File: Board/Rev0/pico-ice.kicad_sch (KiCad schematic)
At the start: 103 parts, among them J1 Connector_USB_B_Micro, J10 2x3_2.54mm_Female, J11 2x3_2.54mm_Female, J3 6X2 Female Header, J4 6X2 Female Header, J5 Conn_ARM_JTAG_SWD_10, J6 6X2 Female Header, J7 6X2 Female Header, J8 6X2 Female Header, J9 BOOT_SEL, SW1 PTS820 J25K SMTR LFS, SW2 PTS820 J25K SMTR LFS, U1 NCP1117ST33T3G, U2 W25Q32JVSSIQ, U3 RP2040, U4 CL9293A12L5M, U5 APS6404L-3SQN-SN, U6 ICE40UP5K-SG48ITR, U8 W25Q32JVSSIQ, Y1 ABLS-12.000MHZ-B4-T

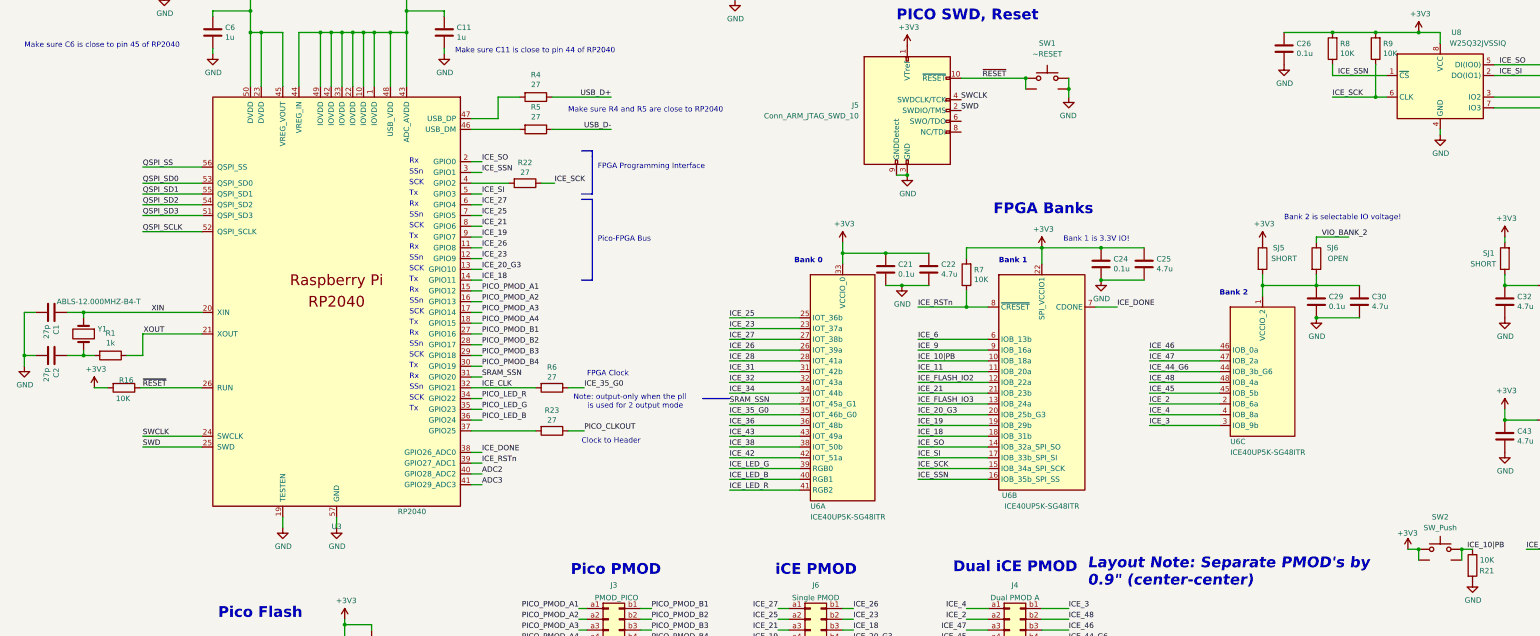
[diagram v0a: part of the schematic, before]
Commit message: Reduce the board outline.
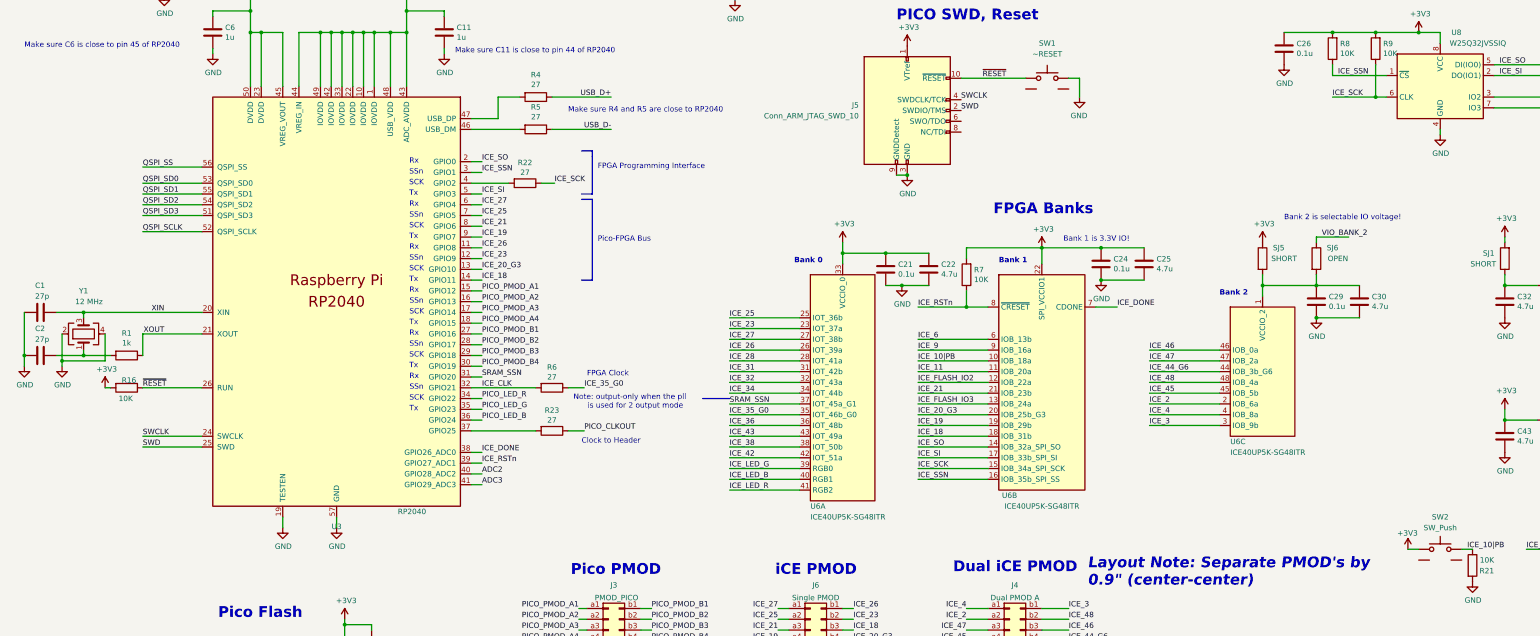
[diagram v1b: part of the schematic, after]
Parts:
- removed Y1: ABLS-12.000MHZ-B4-T, RP2040_minimal:Crystal_SMD_HC49-US, symbol Device:Crystal
- added Y1: 12 MHz, Crystal:Crystal_SMD_2520-4Pin_2.5x2.0mm, symbol Device:Crystal_GND24
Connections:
- net +3V3: no longer SW2.SH1
- net GND: now also Y1.2, Y1.4; no longer SW1.SH1
- net ICE_10|PB: no longer SW2.SH2
- net XIN: now also Y1.3
- net ~{RESET}: no longer SW1.SH2
- net at C2.1, R1.2: now also Y1.1
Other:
- moved on the sheet: C1, C2, R1, R16

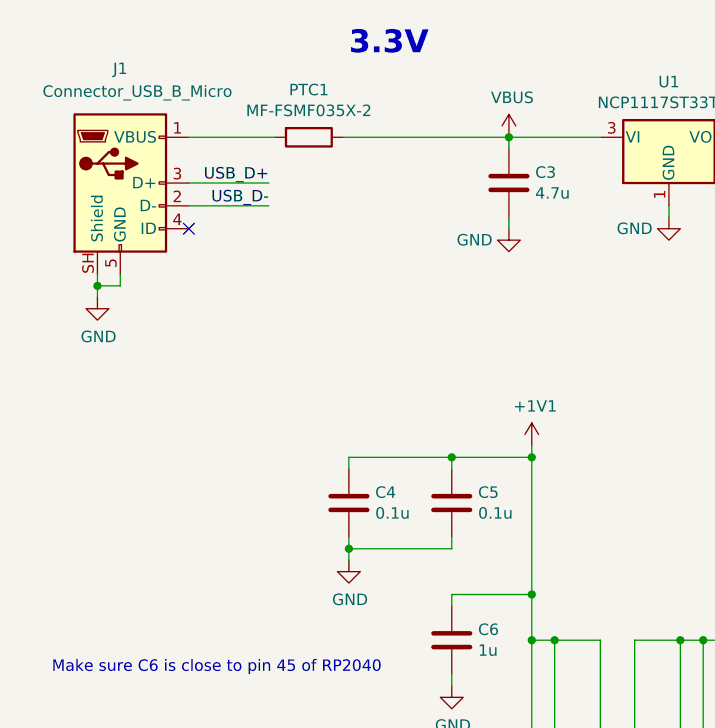
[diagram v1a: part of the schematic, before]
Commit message: Replaced USB connector.
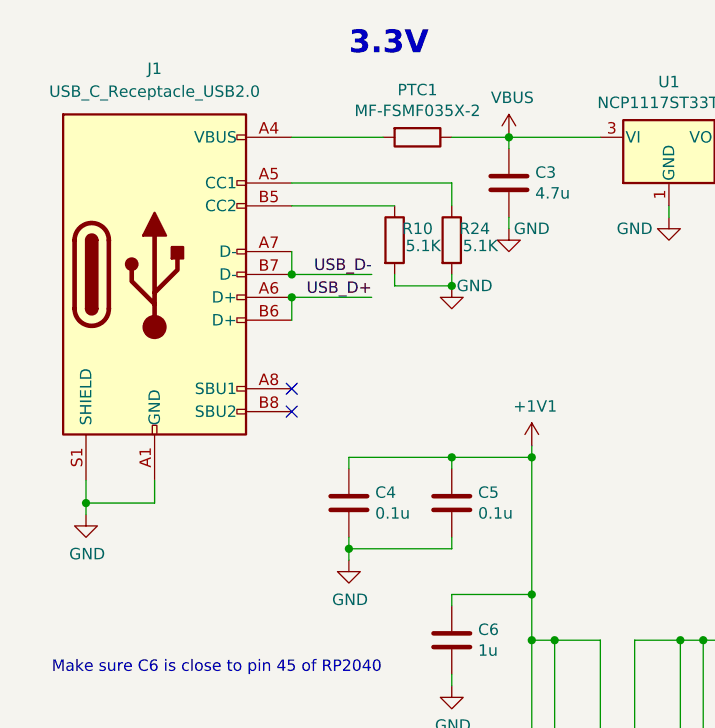
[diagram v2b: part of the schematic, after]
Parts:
- removed J1: Connector_USB_B_Micro, CUSTOM:MOLEX_47589-0001, symbol UPduino_v3.0:Connector_USB_B_Micro
- added J1: USB_C_Receptacle_USB2.0, Connector_USB:USB_C_Receptacle_HRO_TYPE-C-31-M-12, symbol Connector:USB_C_Receptacle_USB2.0
- added R10, R24: 5.1K, Resistor_SMD:R_0402_1005Metric, symbol UPduino_v3.0:Device_R
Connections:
- net GND: now also J1.A1 (GND), J1.A12 (GND), J1.B1 (GND), J1.B12 (GND), J1.S1 (SHIELD), R10.2, R24.2
- net USB_D+: now also J1.A6 (D+), J1.B6 (D+)
- net USB_D-: now also J1.A7 (D-), J1.B7 (D-)
- net at PTC1.2: now also J1.A4 (VBUS), J1.A9 (VBUS), J1.B4 (VBUS), J1.B9 (VBUS)
- new net: J1.A5 (CC1), R24.1
- new net: J1.B5 (CC2), R10.1
- no-connect marks 1 -> 2
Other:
- moved on the sheet: PTC1

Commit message: Synced the latest design files.
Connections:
- net GND: now also SW1.SH1, SW1.SH2, SW2.SH1, SW2.SH2
- net USB_P: now reaches R4.2, U3.47 (USB_DP)
- net USB_N: now reaches R5.2, U3.46 (USB_DM)
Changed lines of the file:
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@@
   (junction (at 279.4 31.75) (diameter 0) (color 0 0 0 0)
   )
+  (junction (at 264.16 97.155) (diameter 0) (color 0 0 0 0)
+  )
   (junction (at 138.43 38.1) (diameter 0) (color 0 0 0 0)
   )
@@
   (junction (at 105.41 83.82) (diameter 0) (color 0 0 0 0)
   )
+  (junction (at 344.17 212.09) (diameter 0) (color 0 0 0 0)
+  )
   (junction (at 95.25 83.82) (diameter 0) (color 0 0 0 0)
   )
@@
     (stroke (width 0) (type default) (color 0 0 0 0))
   )
+  (wire (pts (xy 354.33 212.09) (xy 344.17 212.09))
+    (stroke (width 0) (type default) (color 0 0 0 0))
+  )
   (wire (pts (xy 240.03 267.97) (xy 240.03 278.13))
     (stroke (width 0) (type default) (color 0 0 0 0))
   )
+  (wire (pts (xy 354.33 208.28) (xy 354.33 212.09))
+    (stroke (width 0) (type default) (color 0 0 0 0))
+  )
   (wire (pts (xy 139.7 99.06) (xy 153.67 99.06))
     (stroke (width 0) (type default) (color 0 0 0 0))
@@
     (stroke (width 0) (type default) (color 0 0 0 0))
   )
-  (wire (pts (xy 264.16 94.615) (xy 264.16 99.06))
+  (wire (pts (xy 264.16 94.615) (xy 264.16 97.155))
     (stroke (width 0) (type default) (color 0 0 0 0))
   )
@@
     (stroke (width 0) (type default) (color 0 0 0 0))
   )
+  (wire (pts (xy 251.46 97.155) (xy 251.46 99.06))
+    (stroke (width 0) (type default) (color 0 0 0 0))
+  )
   (wire (pts (xy 344.17 50.8) (xy 346.71 50.8))
     (stroke (width 0) (type default) (color 0 0 0 0))
@@
     (stroke (width 0) (type default) (color 0 0 0 0))
   )
+  (wire (pts (xy 264.16 97.155) (xy 264.16 99.06))
+    (stroke (width 0) (type default) (color 0 0 0 0))
+  )
   (wire (pts (xy 120.65 129.54) (xy 123.19 129.54))
     (stroke (width 0) (type default) (color 0 0 0 0))
@@
     (stroke (width 0) (type default) (color 0 0 0 0))
   )
+  (wire (pts (xy 261.62 97.155) (xy 264.16 97.155))
+    (stroke (width 0) (type default) (color 0 0 0 0))
+  )
   (wire (pts (xy 361.95 91.44) (xy 374.65 91.44))
     (stroke (width 0) (type default) (color 0 0 0 0))
@@
     (stroke (width 0) (type default) (color 0 0 0 0))
   )
+  (wire (pts (xy 344.17 212.09) (xy 344.17 213.36))
+    (stroke (width 0) (type default) (color 0 0 0 0))
+  )
   (wire (pts (xy 323.85 99.06) (xy 334.01 99.06))
     (stroke (width 0) (type default) (color 0 0 0 0))
   )
+  (wire (pts (xy 344.17 208.28) (xy 344.17 212.09))
+    (stroke (width 0) (type default) (color 0 0 0 0))
+  )
   (wire (pts (xy 120.65 119.38) (xy 129.54 119.38))
     (stroke (width 0) (type default) (color 0 0 0 0))
@@
     (effects (font (size 1.27 1.27)) (justify left bottom))
   )
+  (label "USB_N" (at 127 106.68 0)
+    (effects (font (size 1.27 1.27)) (justify left bottom))
+  )
   (label "SRAM_SSN" (at 181.61 171.45 0)
     (effects (font (size 1.27 1.27)) (justify left bottom))
@@
     (effects (font (size 1.27 1.27)) (justify left bottom))
   )
+  (label "USB_P" (at 127 99.06 0)
+    (effects (font (size 1.27 1.27)) (justify left bottom))
+  )
   (label "PICO_LED_B" (at 392.43 180.34 0)
     (effects (font (size 1.27 1.27)) (justify left bottom))
@@
     (pin "SH2")
   )
+  (symbol (lib_id "power:GND") (at 251.46 99.06 0) (mirror y) (unit 1)
+    (in_bom yes) (on_board yes)
+    (property "Reference" "#PWR?" (id 0) (at 251.46 105.41 0)
+      (effects (font (size 1.27 1.27)) hide)
+    )
+    (property "Value" "GND" (id 1) (at 251.333 103.4542 0))
+    (property "Footprint" "" (id 2) (at 251.46 99.06 0)
+      (effects (font (size 1.27 1.27)) hide)
+    )
+    (property "Datasheet" "" (id 3) (at 251.46 99.06 0)
+      (effects (font (size 1.27 1.27)) hide)
+    )
+    (pin "1")
+  )
   (symbol (lib_id "UPduino_v3.0:power_GND") (at 257.81 278.13 0) (mirror y) (unit 1)
     (in_bom yes) (on_board yes)
@@
     (pin "2")
   )
+  (symbol (lib_id "UPduino_v3.0:power_GND") (at 344.17 213.36 0) (unit 1)
+    (in_bom yes) (on_board yes)
+    (property "Reference" "#PWR?" (id 0) (at 344.17 219.71 0)
+      (effects (font (size 1.27 1.27)) hide)
+    )
+    (property "Value" "GND" (id 1) (at 344.297 217.7542 0))
+    (property "Footprint" "" (id 2) (at 344.17 213.36 0)
+      (effects (font (size 1.27 1.27)) hide)
+    )
+    (property "Datasheet" "" (id 3) (at 344.17 213.36 0)
+      (effects (font (size 1.27 1.27)) hide)
+    )
+    (pin "1")
+  )
   (symbol (lib_id "UPduino_v3.0:Device_C") (at 148.59 68.58 0) (unit 1)
     (in_bom yes) (on_board yes)
@@
       (reference "#PWR0103") (unit 1) (value "GND") (footprint "")
     )
+    (path "/347194fd-3b23-45dd-9b01-03f73c27d59d"
+      (reference "#PWR?") (unit 1) (value "GND") (footprint "")
+    )
+    (path "/a0646795-824b-4838-bb54-b552bc76efa1"
+      (reference "#PWR?") (unit 1) (value "GND") (footprint "")
+    )
     (path "/00000000-0000-0000-0000-00005ed96b87"

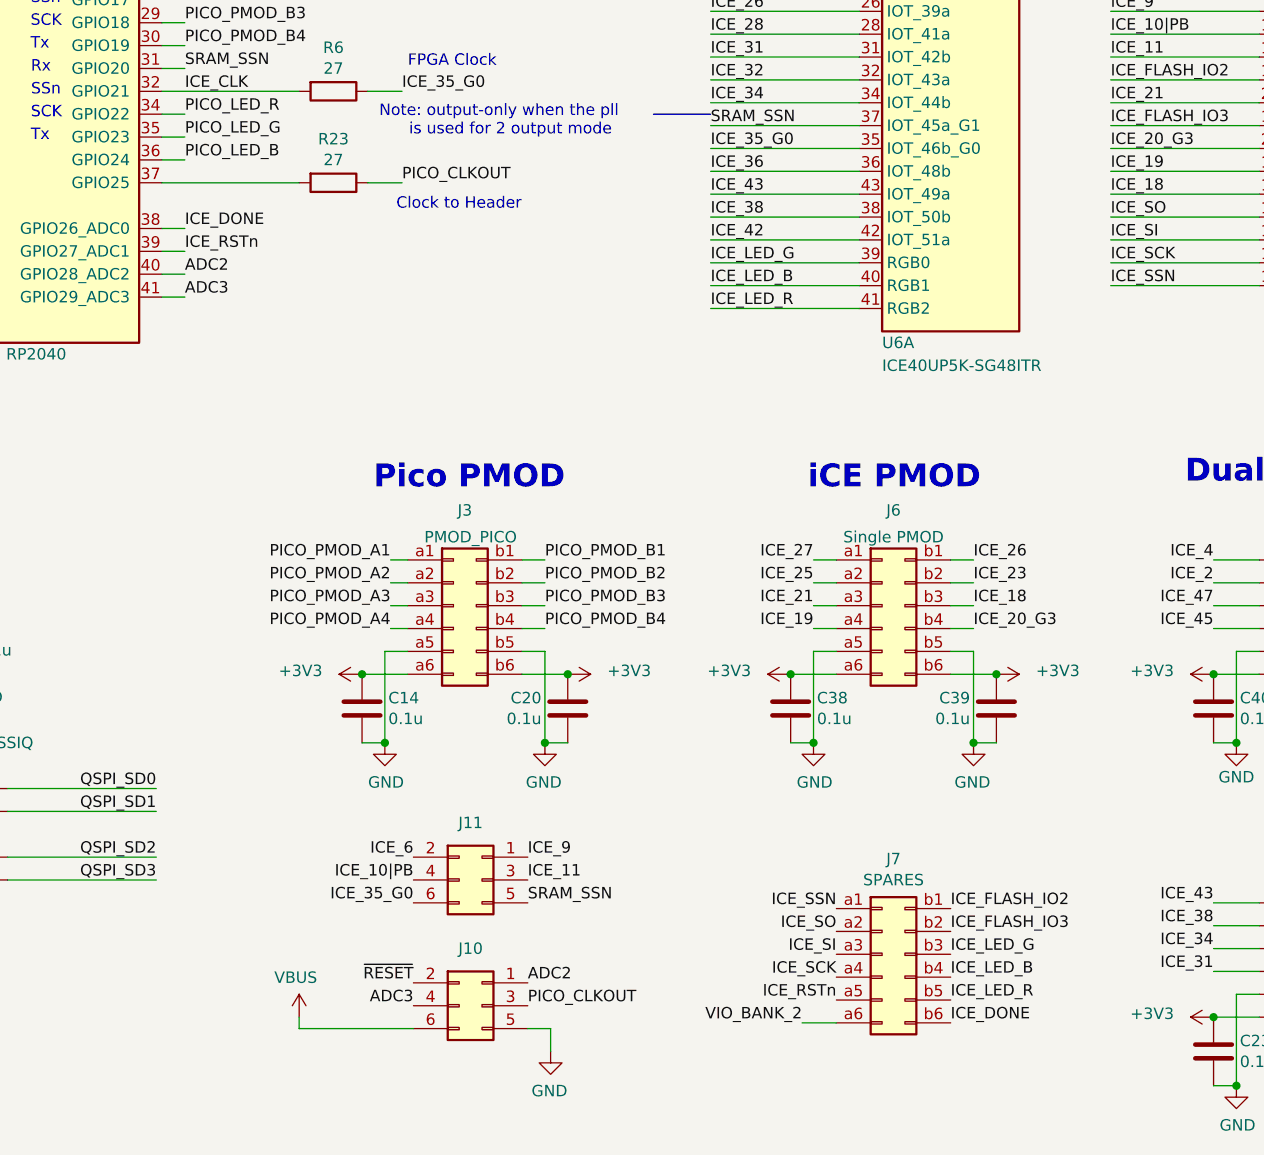
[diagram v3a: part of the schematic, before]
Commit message: Minor changes to pinouts of headers.
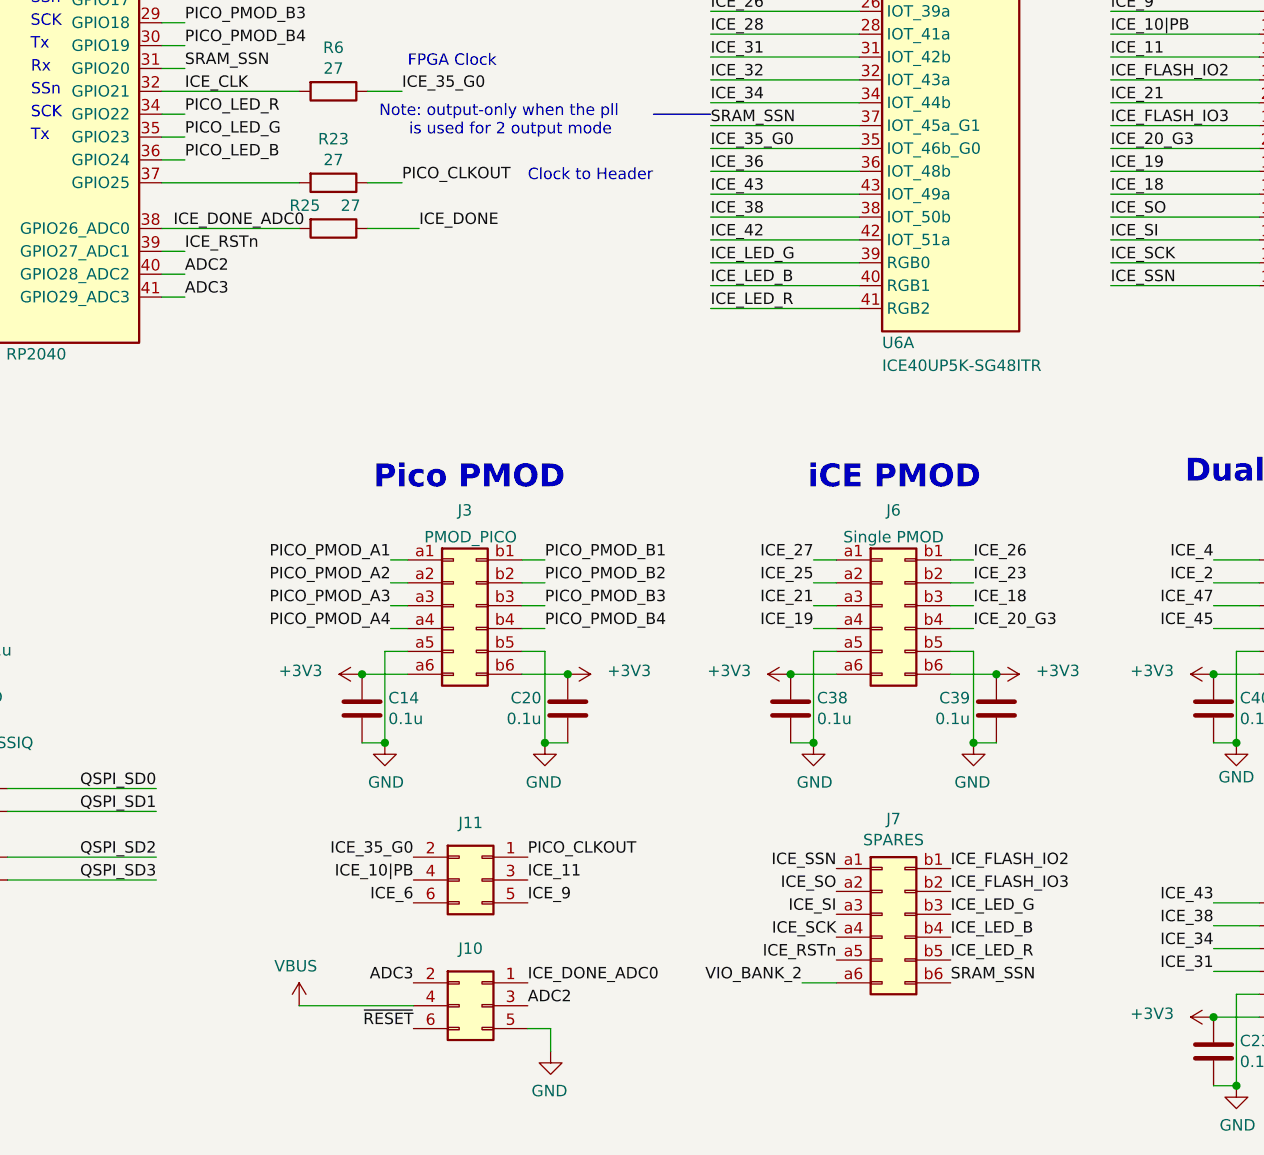
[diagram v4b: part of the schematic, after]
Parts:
- added R25: 27, Resistor_SMD:R_0402_1005Metric, symbol Device:R
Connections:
- net ADC2: now also J10.3; no longer J10.1
- net ADC3: now also J10.2; no longer J10.4
- net ICE_35_G0: now also J11.2; no longer J11.6
- net ICE_6: now also J11.6; no longer J11.2
- net ICE_9: now also J11.5; no longer J11.1
- net ICE_DONE: now also R25.1; no longer J7.b6 (Pin_b6), U3.38 (GPIO26_ADC0)
- net PICO_CLKOUT: now also J11.1; no longer J10.3
- net SRAM_SSN: now also J7.b6 (Pin_b6); no longer J11.5
- net VBUS: now also J10.4; no longer J10.6
- net ~{RESET}: now also J10.6; no longer J10.2
- new net ICE_DONE_ADC0: J10.1, R25.2, U3.38 (GPIO26_ADC0)
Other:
- moved on the sheet: J7

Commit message: Updated the routing.
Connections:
- net ADC2: now also J10.4; no longer J10.3
- net ICE_10|PB: now also J11.1; no longer J11.4
- net ICE_6: now also J11.5; no longer J11.6
- net ICE_9: now also J11.6; no longer J11.5
- net PICO_CLKOUT: now also J11.4; no longer J11.1
- net VBUS: now also J10.3; no longer J10.4
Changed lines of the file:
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@@
     (stroke (width 0) (type default) (color 0 0 0 0))
   )
+  (wire (pts (xy 161.29 269.24) (xy 176.53 269.24))
+    (stroke (width 0) (type default) (color 0 0 0 0))
+  )
   (wire (pts (xy 364.49 140.97) (xy 364.49 143.51))
     (stroke (width 0) (type default) (color 0 0 0 0))
@@
     (stroke (width 0) (type default) (color 0 0 0 0))
   )
+  (wire (pts (xy 176.53 269.24) (xy 176.53 264.16))
+    (stroke (width 0) (type default) (color 0 0 0 0))
+  )
   (wire (pts (xy 297.18 163.83) (xy 280.67 163.83))
     (stroke (width 0) (type default) (color 0 0 0 0))
@@
     (stroke (width 0) (type default) (color 0 0 0 0))
   )
-  (wire (pts (xy 135.89 269.24) (xy 148.59 269.24))
-    (stroke (width 0) (type default) (color 0 0 0 0))
-  )
   (wire (pts (xy 344.17 35.56) (xy 354.33 35.56))
     (stroke (width 0) (type default) (color 0 0 0 0))
@@
     (effects (font (size 1.27 1.27)) (justify left bottom))
   )
-  (label "ICE_6" (at 148.59 257.81 180)
-    (effects (font (size 1.27 1.27)) (justify right bottom))
+  (label "ICE_6" (at 161.29 257.81 0)
+    (effects (font (size 1.27 1.27)) (justify left bottom))
   )
   (label "USB_N" (at 127 106.68 0)
@@
     (effects (font (size 1.27 1.27)) (justify left bottom))
   )
-  (label "PICO_CLKOUT" (at 161.29 252.73 0)
-    (effects (font (size 1.27 1.27)) (justify left bottom))
+  (label "PICO_CLKOUT" (at 148.59 255.27 180)
+    (effects (font (size 1.27 1.27)) (justify right bottom))
   )
   (label "ICE_42" (at 181.61 184.15 0)
@@
     (effects (font (size 1.27 1.27)) (justify left bottom))
   )
-  (label "ICE_10|PB" (at 148.59 255.27 180)
-    (effects (font (size 1.27 1.27)) (justify right bottom))
+  (label "ICE_10|PB" (at 161.29 252.73 0)
+    (effects (font (size 1.27 1.27)) (justify left bottom))
   )
   (label "PICO_CLKOUT" (at 147.32 177.8 0)
@@
     (effects (font (size 1.27 1.27)) (justify right bottom))
   )
-  (label "ICE_9" (at 161.29 257.81 0)
-    (effects (font (size 1.27 1.27)) (justify left bottom))
+  (label "ICE_9" (at 148.59 257.81 180)
+    (effects (font (size 1.27 1.27)) (justify right bottom))
   )
   (label "ICE_27" (at 123.19 124.46 0)
@@
     (effects (font (size 1.27 1.27)) (justify left bottom))
   )
-  (label "ADC2" (at 161.29 269.24 0)
-    (effects (font (size 1.27 1.27)) (justify left bottom))
+  (label "ADC2" (at 148.59 269.24 180)
+    (effects (font (size 1.27 1.27)) (justify right bottom))
   )
   (label "ICE_48" (at 280.67 166.37 0)
@@
     (pin "SH2")
   )
-  (symbol (lib_id "power:VBUS") (at 135.89 269.24 0) (mirror y) (unit 1)
+  (symbol (lib_id "power:VBUS") (at 176.53 264.16 0) (mirror y) (unit 1)
     (in_bom yes) (on_board yes)
-    (property "Reference" "#PWR0101" (id 0) (at 135.89 273.05 0)
+    (property "Reference" "#PWR0101" (id 0) (at 176.53 267.97 0)
       (effects (font (size 1.27 1.27)) hide)
     )
-    (property "Value" "VBUS" (id 1) (at 135.509 264.8458 0))
-    (property "Footprint" "" (id 2) (at 135.89 269.24 0)
+    (property "Value" "VBUS" (id 1) (at 176.149 259.7658 0))
+    (property "Footprint" "" (id 2) (at 176.53 264.16 0)
       (effects (font (size 1.27 1.27)) hide)
     )
-    (property "Datasheet" "" (id 3) (at 135.89 269.24 0)
+    (property "Datasheet" "" (id 3) (at 176.53 264.16 0)
       (effects (font (size 1.27 1.27)) hide)
     )
